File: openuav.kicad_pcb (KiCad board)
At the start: 4 copper layers, 36 x 36 mm, 73 parts, among them J1 Conn_01x01, J10 Conn_01x01, J11 Conn_01x01, J12 Conn_01x01, J13 Conn_01x01, J14 Conn_01x01, J15 Conn_01x01, J16 Conn_01x01, J17 Conn_01x01, J18 Conn_01x01, J19 Conn_01x01, J2 Conn_01x01, J20 Conn_01x01, J21 Conn_01x01, J22 Conn_01x01, J23 Conn_01x01, J24 Conn_01x01, J25 Conn_01x01, J26 Conn_01x01, J27 Conn_01x01, J28 Conn_01x01, J29 Conn_01x01, J3 Conn_01x01, J30 Conn_01x01, J31 Conn_01x01, J32 Conn_01x01, J33 Conn_01x01, J34 Conn_01x01, J35 Conn_01x01, J36 Conn_01x01, J37 Conn_01x01, J4 Conn_01x01, J5 Conn_01x01, J6 Conn_01x01, J7 Conn_01x01, J8 Conn_01x01, J9 Conn_01x01, J99 USB_C_Receptacle_USB2.0, U1 STM32G431CBUx, U3 LSM6DSR, U4 LPS22HH, U5 TPS54202DDC, U6 W25N01GVZEIG, U7 XC6206P332MR

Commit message: update ioc file with all pins, add pulldown on boot0
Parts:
- added R8: 10k, Resistor_SMD:R_0402_1005Metric, F.Cu at (138.1, 58.9)
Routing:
- net BOOT0: track 19.4 -> 21.4 mm, vias 1 -> 2
- net GND: track 24.4 -> 25.6 mm
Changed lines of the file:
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@@
       (net 2 "GND") (pinfunction "Pin_1") (pintype "passive"))
+  )
+  (footprint "Resistor_SMD:R_0402_1005Metric" (layer "F.Cu")
+    (at 138.1 58.9 180)
+    (descr "Resistor SMD 0402 (1005 Metric), square (rectangular) end terminal, IPC_7351 nominal, (Body size source: IPC-SM-782 page 72, https://www.pcb-3d.com/wordpress/wp-content/uploads/ipc-sm-782a_amendment_1_and_2.pdf), generated with kicad-footprint-generator")
+    (tags "resistor")
+    (property "LCSC" "C17414")
+    (property "Sheetfile" "openuav.kicad_sch")
+    (property "Sheetname" "")
+    (property "ki_description" "Resistor, small symbol")
+    (property "ki_keywords" "R resistor")
+    (attr smd)
+    (fp_text reference "R8" (at 0 -1.17) (layer "F.SilkS") hide
+        (effects (font (size 1 1) (thickness 0.15)))
+    )
+    (fp_text value "10k" (at 0 1.17) (layer "F.Fab")
+        (effects (font (size 1 1) (thickness 0.15)))
+    )
+    (fp_text user "${REFERENCE}" (at 0 0) (layer "F.Fab")
+        (effects (font (size 0.26 0.26) (thickness 0.04)))
+    )
+    (fp_line (start -0.153641 -0.38) (end 0.153641 -0.38)
+      (stroke (width 0.12) (type solid)) (layer "F.SilkS"))
+    (fp_line (start -0.153641 0.38) (end 0.153641 0.38)
+      (stroke (width 0.12) (type solid)) (layer "F.SilkS"))
+    (fp_line (start -0.93 -0.47) (end 0.93 -0.47)
+      (stroke (width 0.05) (type solid)) (layer "F.CrtYd"))
+    (fp_line (start -0.93 0.47) (end -0.93 -0.47)
+      (stroke (width 0.05) (type solid)) (layer "F.CrtYd"))
+    (fp_line (start 0.93 -0.47) (end 0.93 0.47)
+      (stroke (width 0.05) (type solid)) (layer "F.CrtYd"))
+    (fp_line (start 0.93 0.47) (end -0.93 0.47)
+      (stroke (width 0.05) (type solid)) (layer "F.CrtYd"))
+    (fp_line (start -0.525 -0.27) (end 0.525 -0.27)
+      (stroke (width 0.1) (type solid)) (layer "F.Fab"))
+    (fp_line (start -0.525 0.27) (end -0.525 -0.27)
+      (stroke (width 0.1) (type solid)) (layer "F.Fab"))
+    (fp_line (start 0.525 -0.27) (end 0.525 0.27)
+      (stroke (width 0.1) (type solid)) (layer "F.Fab"))
+    (fp_line (start 0.525 0.27) (end -0.525 0.27)
+      (stroke (width 0.1) (type solid)) (layer "F.Fab"))
+    (pad "1" smd roundrect (at -0.51 0 180) (size 0.54 0.64) (layers "F.Cu" "F.Paste" "F.Mask") (roundrect_rratio 0.25)
+      (net 28 "BOOT0") (pintype "passive"))
+    (pad "2" smd roundrect (at 0.51 0 180) (size 0.54 0.64) (layers "F.Cu" "F.Paste" "F.Mask") (roundrect_rratio 0.25)
+      (net 2 "GND") (pintype "passive"))
+    (model "${KICAD6_3DMODEL_DIR}/Resistor_SMD.3dshapes/R_0402_1005Metric.wrl"
+      (offset (xyz 0 0 0))
+      (scale (xyz 1 1 1))
+      (rotate (xyz 0 0 0))
+    )
   )
   (footprint "Package_LGA:ST_HLGA-10_2x2mm_P0.5mm_LayoutBorder3x2y" (layer "F.Cu")
@@
       (net 26 "UART_1_TX") (pinfunction "PC4") (pintype "bidirectional"))
     (pad "17" smd roundrect (at -0.75 3.4375 90) (size 0.25 0.875) (layers "F.Cu" "F.Paste" "F.Mask") (roundrect_rratio 0.25)
-      (net 1 "unconnected-(U1-PB0-Pad17)") (pinfunction "PB0") (pintype "bidirectional"))
+      (net 1 "unconnected-(U1-PB0-Pad17)") (pinfunction "PB0") (pintype "bidirectional+no_connect"))
     (pad "18" smd roundrect (at -0.25 3.4375 90) (size 0.25 0.875) (layers "F.Cu" "F.Paste" "F.Mask") (roundrect_rratio 0.25)
       (net 50 "SPI1_CS") (pinfunction "PB1") (pintype "bidirectional"))
@@
   (segment (start 156.12 69.2) (end 155.3 69.2) (width 0.254) (layer "F.Cu") (net 2))
   (segment (start 151.1 59) (end 151.1 57.8) (width 0.254) (layer "F.Cu") (net 2))
+  (segment (start 137.58 60.1) (end 137.58 58.91) (width 0.254) (layer "F.Cu") (net 2))
   (segment (start 144.2 57.8) (end 144.9 57.8) (width 0.254) (layer "F.Cu") (net 2))
   (segment (start 139.61 69.83) (end 139.58 69.8) (width 0.254) (layer "F.Cu") (net 2))
@@
   (segment (start 154.404 62.926) (end 154.404 64.378) (width 0.254) (layer "F.Cu") (net 2))
   (segment (start 140.42 69.83) (end 139.61 69.83) (width 0.254) (layer "F.Cu") (net 2))
+  (segment (start 137.58 58.91) (end 137.59 58.9) (width 0.254) (layer "F.Cu") (net 2))
   (segment (start 144.9 59.14) (end 144.9 57.8) (width 0.254) (layer "F.Cu") (net 2))
   (segment (start 157.99 74.3575) (end 157.99 73.1875) (width 0.6) (layer "F.Cu") (net 2))
@@
   (segment (start 154.112764 61.4) (end 151.916264 61.4) (width 0.254) (layer "B.Cu") (net 27))
   (segment (start 145.3125 67.15) (end 144.25 67.15) (width 0.254) (layer "F.Cu") (net 28))
+  (segment (start 138.61 58.9) (end 140.6 58.9) (width 0.254) (layer "F.Cu") (net 28))
   (segment (start 144.25 67.15) (end 144.2 67.2) (width 0.254) (layer "F.Cu") (net 28))
+  (segment (start 140.6 58.9) (end 140.655291 58.844709) (width 0.254) (layer "F.Cu") (net 28))
   (via (at 144.2 67.2) (size 0.5) (drill 0.25) (layers "F.Cu" "B.Cu") (net 28))
+  (via (at 140.655291 58.844709) (size 0.5) (drill 0.25) (layers "F.Cu" "B.Cu") (net 28))
+  (segment (start 139.192 57.381418) (end 140.655291 58.844709) (width 0.254) (layer "B.Cu") (net 28))
   (segment (start 137.922 51.562) (end 139.192 52.832) (width 0.254) (layer "B.Cu") (net 28))
+  (segment (start 140.655291 58.844709) (end 143.196 61.385418) (width 0.254) (layer "B.Cu") (net 28))
   (segment (start 143.196 61.385418) (end 143.196 61.722) (width 0.254) (layer "B.Cu") (net 28))
-  (segment (start 139.192 57.381418) (end 143.196 61.385418) (width 0.254) (layer "B.Cu") (net 28))
   (segment (start 144.2 67.2) (end 143.196 66.196) (width 0.254) (layer "B.Cu") (net 28))
   (segment (start 143.196 66.196) (end 143.196 61.722) (width 0.254) (layer "B.Cu") (net 28))

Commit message: final touches to pcb
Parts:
- added REF**: OSHW-Logo2_7.3x6mm_SilkScreen, Symbol:OSHW-Logo2_7.3x6mm_SilkScreen, B.Cu at (137.2, 64.6)
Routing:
- net UART_4_TX: track 16.8 -> 17.6 mm
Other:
- board text added: "JLCJLCJLCJLC"
- board text added: "v0.1"

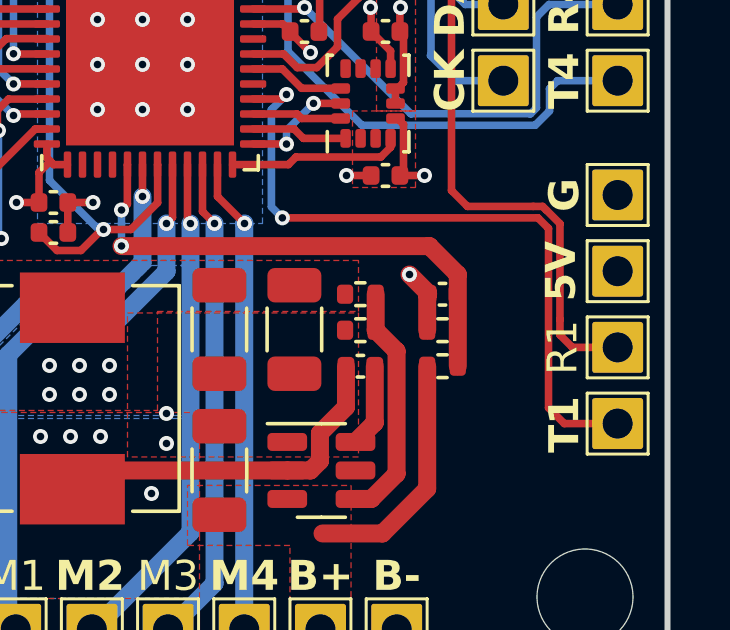
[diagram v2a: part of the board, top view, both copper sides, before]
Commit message: add note about TT pin
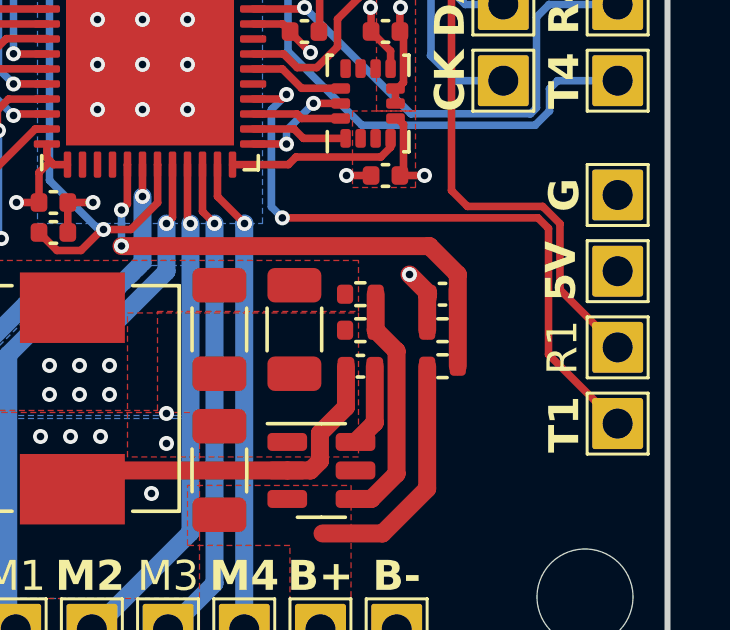
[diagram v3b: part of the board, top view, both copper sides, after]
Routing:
- net UART_1_TX: track 23.2 -> 22.1 mm
- net UART_1_RX: track 29.4 -> 28.5 mm
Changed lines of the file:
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@@
   (segment (start 145.3125 63.15) (end 142.163 63.15) (width 0.254) (layer "F.Cu") (net 25))
   (segment (start 131.572 63.754) (end 136.246 63.754) (width 0.254) (layer "F.Cu") (net 25))
-  (segment (start 153.162 70.612) (end 161.681 70.612) (width 0.254) (layer "F.Cu") (net 26))
-  (segment (start 161.681 70.612) (end 162.0345 70.9655) (width 0.254) (layer "F.Cu") (net 26))
   (segment (start 153.15 66.65) (end 153.3 66.5) (width 0.254) (layer "F.Cu") (net 26))
-  (segment (start 162.56 77.47) (end 164.338 77.47) (width 0.254) (layer "F.Cu") (net 26))
-  (segment (start 162.0345 70.9655) (end 162.0345 76.9445) (width 0.254) (layer "F.Cu") (net 26))
+  (segment (start 162.0345 70.9655) (end 161.681 70.612) (width 0.254) (layer "F.Cu") (net 26))
+  (segment (start 162.0345 75.1665) (end 162.0345 70.9655) (width 0.254) (layer "F.Cu") (net 26))
   (segment (start 152.1875 66.65) (end 153.15 66.65) (width 0.254) (layer "F.Cu") (net 26))
-  (segment (start 162.0345 76.9445) (end 162.56 77.47) (width 0.254) (layer "F.Cu") (net 26))
+  (segment (start 161.681 70.612) (end 153.162 70.612) (width 0.254) (layer "F.Cu") (net 26))
+  (segment (start 164.338 77.47) (end 162.0345 75.1665) (width 0.254) (layer "F.Cu") (net 26))
   (via (at 153.3 66.5) (size 0.5) (drill 0.25) (layers "F.Cu" "B.Cu") (net 26))
   (via (at 153.162 70.612) (size 0.5) (drill 0.25) (layers "F.Cu" "B.Cu") (net 26))
@@
   (segment (start 153.162 70.612) (end 152.796 70.246) (width 0.254) (layer "B.Cu") (net 26))
   (segment (start 152.796 70.246) (end 152.796 67.004) (width 0.254) (layer "B.Cu") (net 26))
-  (segment (start 161.953908 70.346092) (end 161.838815 70.231) (width 0.254) (layer "F.Cu") (net 27))
-  (segment (start 162.4155 74.5155) (end 162.4155 74) (width 0.254) (layer "F.Cu") (net 27))
+  (segment (start 158.8 69.7) (end 158.8 63.2) (width 0.254) (layer "F.Cu") (net 27))
+  (segment (start 164.338 74.93) (end 162.4155 73.0075) (width 0.254) (layer "F.Cu") (net 27))
   (segment (start 148 61.9625) (end 148 60.9035) (width 0.254) (layer "F.Cu") (net 27))
-  (segment (start 164.338 74.93) (end 162.83 74.93) (width 0.254) (layer "F.Cu") (net 27))
-  (segment (start 162.4155 70.807684) (end 161.953908 70.346092) (width 0.254) (layer "F.Cu") (net 27))
+  (segment (start 162.4155 70.807684) (end 161.838815 70.231) (width 0.254) (layer "F.Cu") (net 27))
+  (segment (start 158.2 62.6) (end 156.4 62.6) (width 0.254) (layer "F.Cu") (net 27))
+  (segment (start 161.838815 70.231) (end 159.331 70.231) (width 0.254) (layer "F.Cu") (net 27))
+  (segment (start 148 60.9035) (end 148.0035 60.9) (width 0.254) (layer "F.Cu") (net 27))
   (segment (start 158.8 63.2) (end 158.2 62.6) (width 0.254) (layer "F.Cu") (net 27))
-  (segment (start 162.4155 74) (end 162.4155 70.807684) (width 0.254) (layer "F.Cu") (net 27))
-  (segment (start 158.2 62.6) (end 156.4 62.6) (width 0.254) (layer "F.Cu") (net 27))
   (segment (start 159.331 70.231) (end 158.8 69.7) (width 0.254) (layer "F.Cu") (net 27))
-  (segment (start 162.83 74.93) (end 162.4155 74.5155) (width 0.254) (layer "F.Cu") (net 27))
-  (segment (start 158.8 69.7) (end 158.8 63.2) (width 0.254) (layer "F.Cu") (net 27))
-  (segment (start 148 60.9035) (end 148.0035 60.9) (width 0.254) (layer "F.Cu") (net 27))
-  (segment (start 161.838815 70.231) (end 161.523184 70.231) (width 0.254) (layer "F.Cu") (net 27))
-  (segment (start 161.523184 70.231) (end 159.331 70.231) (width 0.254) (layer "F.Cu") (net 27))
+  (segment (start 162.4155 73.0075) (end 162.4155 70.807684) (width 0.254) (layer "F.Cu") (net 27))
   (via (at 148.0035 60.9) (size 0.5) (drill 0.25) (layers "F.Cu" "B.Cu") (net 27))
   (via (at 156.4 62.6) (size 0.5) (drill 0.25) (layers "F.Cu" "B.Cu") (net 27))

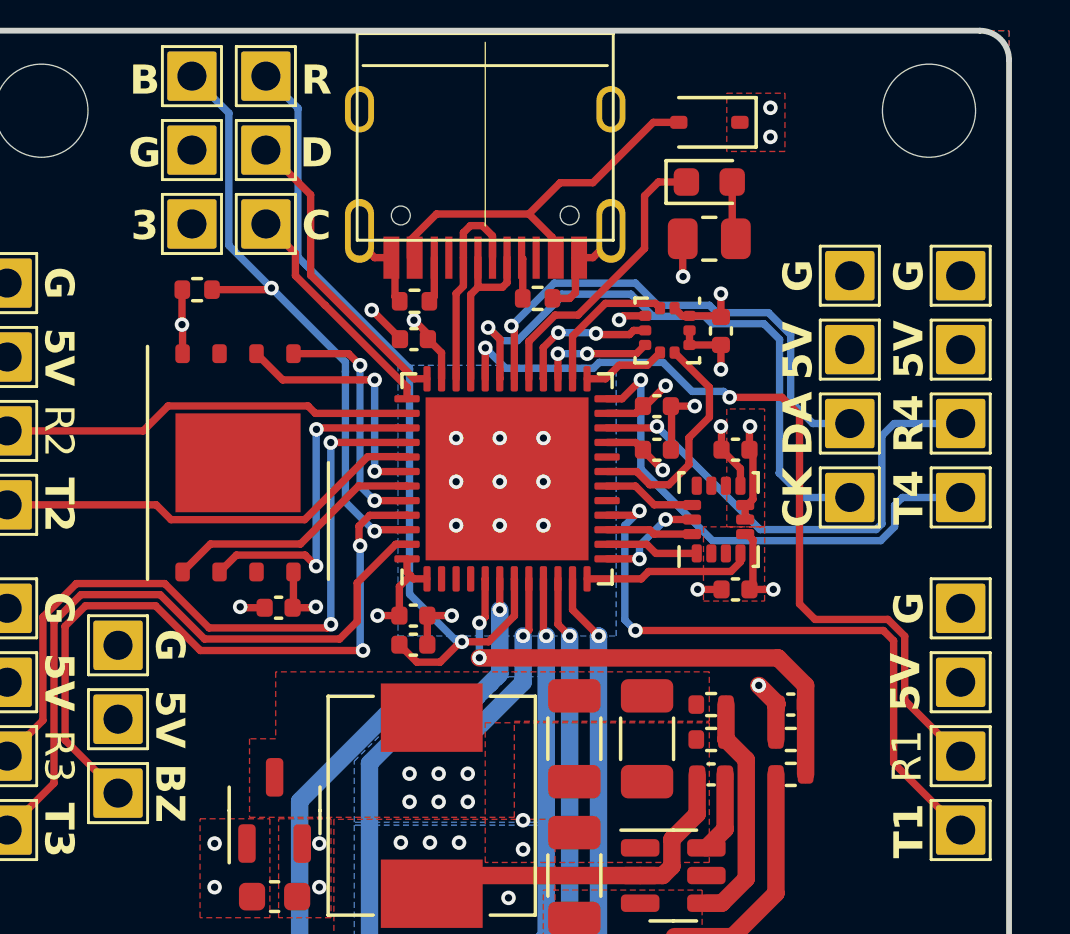
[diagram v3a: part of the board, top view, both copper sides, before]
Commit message: Replace ST parts with BMI270 and BMP280
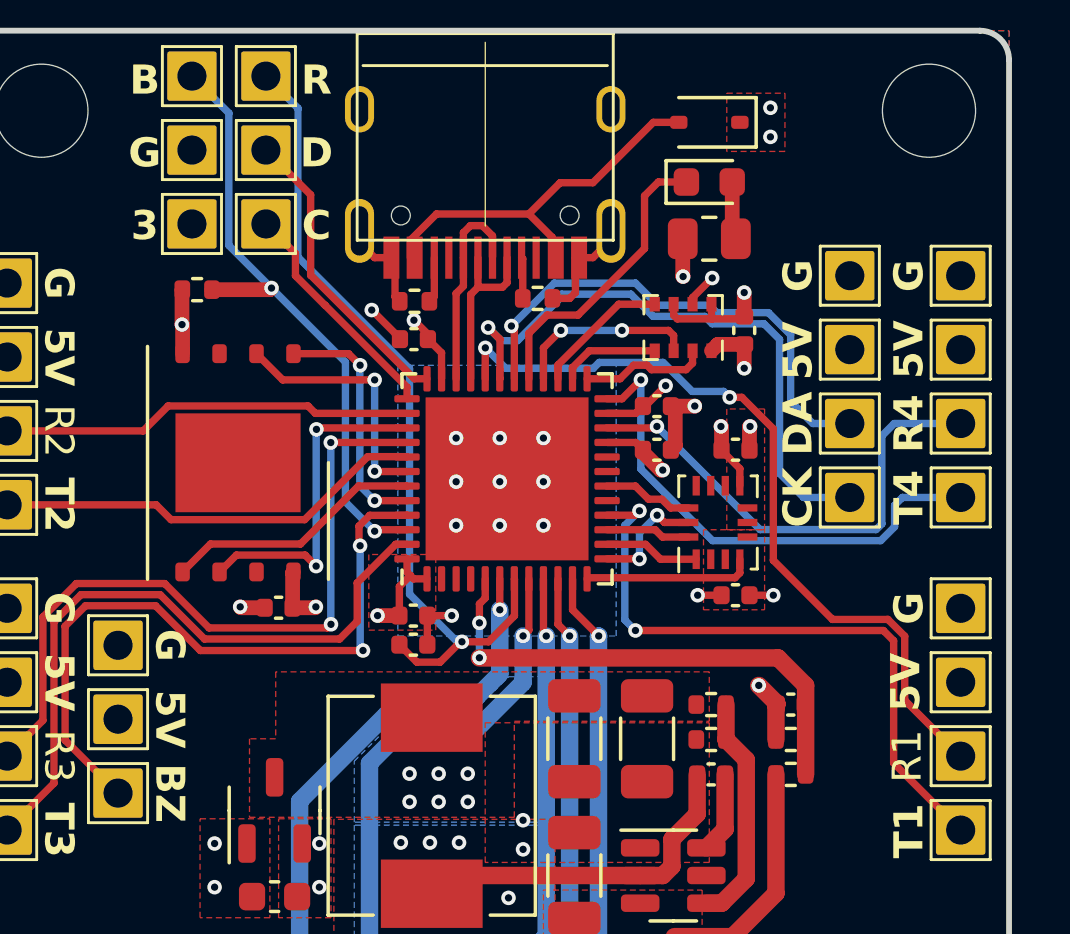
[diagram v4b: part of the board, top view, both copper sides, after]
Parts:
- removed U4: LPS22HH, Package_LGA:ST_HLGA-10_2x2mm_P0.5mm_LayoutBorder3x2y
- added U2: BMI270, Package_LGA:Bosch_LGA-14_3x2.5mm_P0.5mm, F.Cu at (156.0, 66.9)
- U3: value LSM6DSR -> BMP280; footprint Package_LGA:LGA-14_3x2.5mm_P0.5mm_LayoutBorder3x4y -> Package_LGA:Bosch_LGA-8_2x2.5mm_P0.65mm_ClockwisePinNumbering
- moved U3 6.71 mm to (154.8, 60.2), turned to 180 degrees
- moved C12 0.80 mm to (156.9, 60.3)
- moved C11 0.20 mm to (156.6, 69.4)
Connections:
- U3 pad 1: SPI1_MISO -> GND
- U3 pad 2: +3V3 -> SPI2_CS
- U3 pad 3: +3V3 -> SPI2_MOSI
- U3 pad 4: GYRO_INT -> SPI2_CLK
- U3 pad 5: +3V3 -> SPI2_MISO
- U3 pad 6: GND -> +3V3
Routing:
- net BARO_INT: track 7.92 -> 0.00 mm
- net GND: track 25.6 -> 23.0 mm
- net SPI2_CLK: track 5.01 -> 3.45 mm
- net SPI2_CS: track 2.88 -> 4.40 mm
- net SPI2_MOSI: track 4.88 -> 6.38 mm
- net UART_1_RX: track 28.5 -> 27.3 mm
- net SPI2_MISO: track 3.99 -> 4.66 mm, vias 2 -> 0

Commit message: Add missing JLC part numbers
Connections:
- U1 pad 19: BARO_INT -> unconnected-(U1-PB2-Pad19)
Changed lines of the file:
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@@
   (net 31 "SPI2_MISO")
   (net 32 "GYRO_INT")
-  (net 33 "BARO_INT")
+  (net 33 "unconnected-(U1-PB2-Pad19)")
   (net 34 "unconnected-(U5-EN-Pad5)")
   (net 35 "unconnected-(U6-IO2-Pad3)")
@@
     (descr "LGA-14 Bosch https://ae-bst.resource.bosch.com/media/_tech/media/datasheets/BST-BMI160-DS000-07.pdf")
     (tags "lga land grid array")
+    (property "LCSC" "C2836813")
     (property "Sheetfile" "openuav.kicad_sch")
     (property "Sheetname" "")
@@
     (descr "LGA-8, https://ae-bst.resource.bosch.com/media/_tech/media/datasheets/BST-BMP280-DS001-18.pdf")
     (tags "lga land grid array")
+    (property "LCSC" "C83291")
     (property "Sheetfile" "openuav.kicad_sch")
     (property "Sheetname" "")
@@
       (net 47 "SPI1_CS") (pinfunction "PB1") (pintype "bidirectional"))
     (pad "19" smd roundrect (at 0.25 3.4375 90) (size 0.25 0.875) (layers "F.Cu" "F.Paste" "F.Mask") (roundrect_rratio 0.25)
-      (net 33 "BARO_INT") (pinfunction "PB2") (pintype "bidirectional"))
+      (net 33 "unconnected-(U1-PB2-Pad19)") (pinfunction "PB2") (pintype "bidirectional+no_connect"))
     (pad "20" smd roundrect (at 0.75 3.4375 90) (size 0.25 0.875) (layers "F.Cu" "F.Paste" "F.Mask") (roundrect_rratio 0.25)
       (net 19 "unconnected-(U1-VREF+-Pad20)") (pinfunction "VREF+") (pintype "input+no_connect"))
@@
     (descr "Resistor SMD 0402 (1005 Metric), square (rectangular) end terminal, IPC_7351 nominal, (Body size source: IPC-SM-782 page 72, https://www.pcb-3d.com/wordpress/wp-content/uploads/ipc-sm-782a_amendment_1_and_2.pdf), generated with kicad-footprint-generator")
     (tags "resistor")
-    (property "LCSC" "C852522")
-    (property "Sheetfile" "openuav.kicad_sch")
-    (property "Sheetname" "")
+    (property "LCSC" "C25854")
+    (property "Sheetfile" "openuav.kicad_sch")
+    (property "Sheetname" "")
